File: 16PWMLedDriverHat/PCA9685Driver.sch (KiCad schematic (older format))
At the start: 17 parts, among them P1 C A0 A1 A2 A3 A4 A5 A6 A7, P2 C B0 B1 B2 B3 B4 B5 B6 B7, U1 PCA9685, U2 TBD62X83A, U3 TBD62X83A

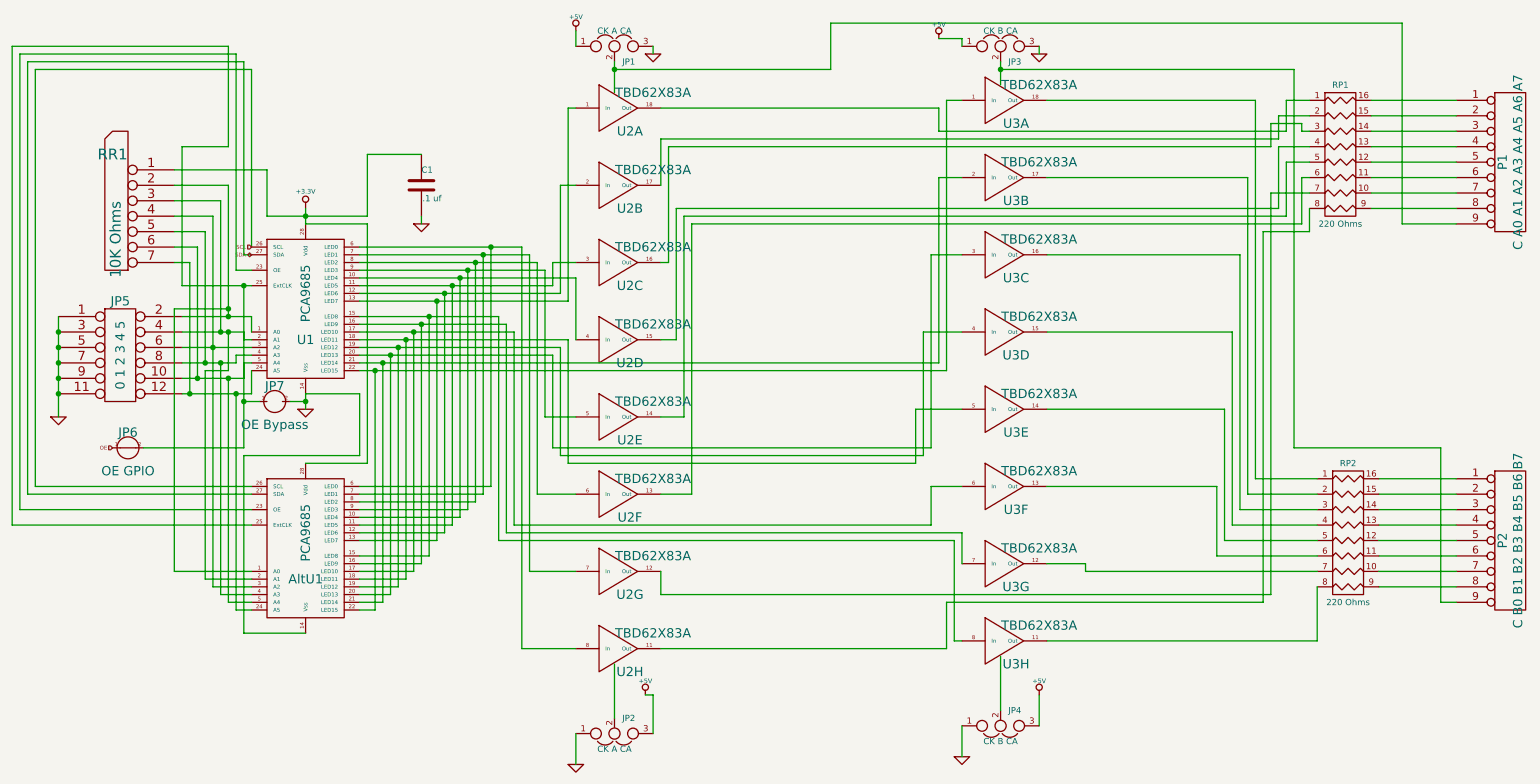
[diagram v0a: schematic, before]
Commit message: Convert the 16PWM Led Drivers to use 12V for the LEDs.
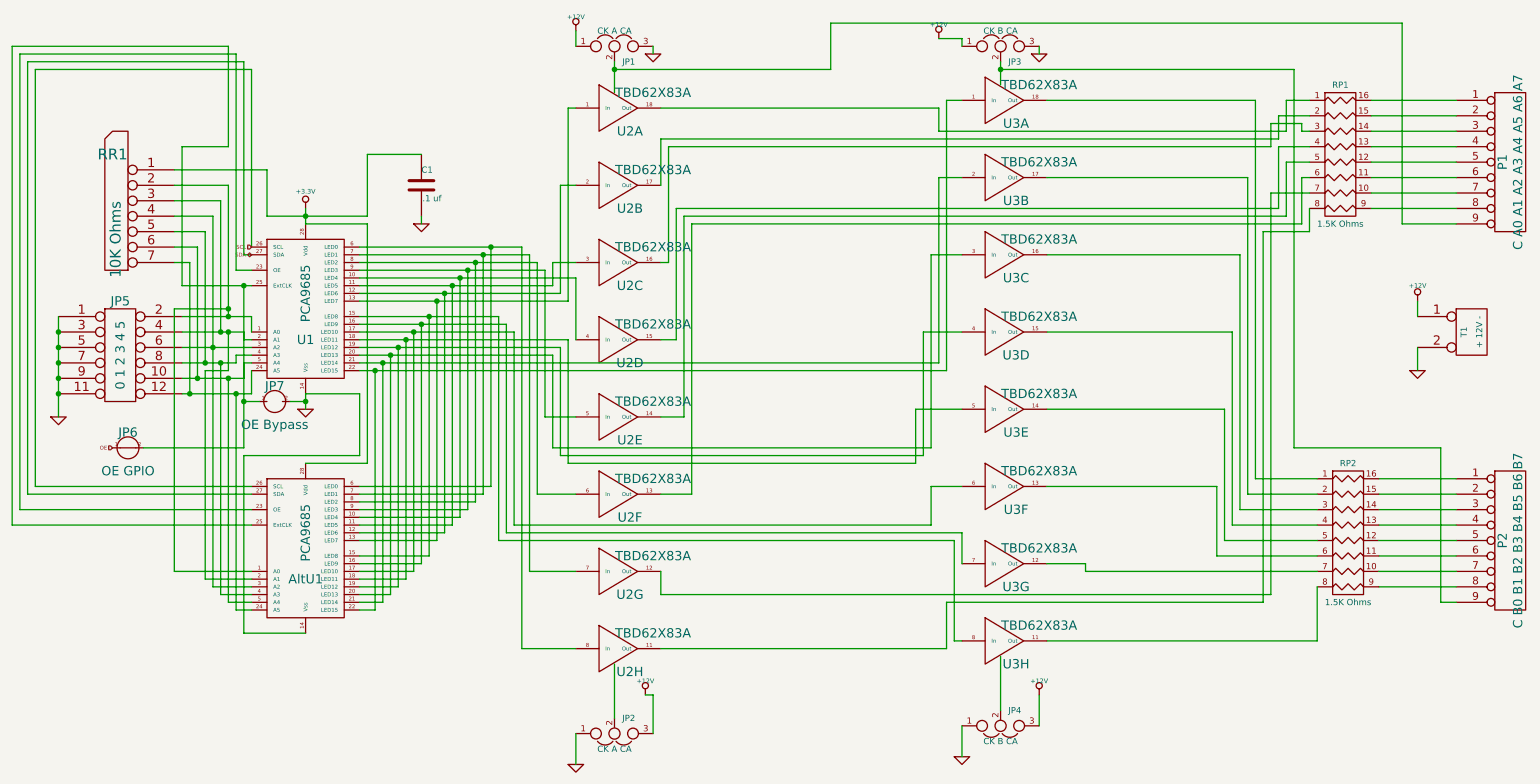
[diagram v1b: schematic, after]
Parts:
- added T1: + 12V -, symbol CONN_2
- RP1, RP2: value 220 Ohms -> 1.5K Ohms
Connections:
- net GND: now also T1.2 (PM)
- net +5V renamed +12V
- net +12V: now also T1.1 (P1)
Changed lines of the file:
@@
 Sheet 2 2
 Title ""
-Date "10 mar 2019"
+Date "28 mar 2019"
 Rev ""
 Comp ""
@@
 P 9500 1400
 F 0 "RP1" H 9500 1850 40  0000 C CNN
-F 1 "220 Ohms" H 9500 950 40  0000 C CNN
+F 1 "1.5K Ohms" H 9500 950 40  0000 C CNN
 F 2 "~" H 9500 1400 60  0000 C CNN
 F 3 "~" H 9500 1400 60  0000 C CNN
@@
 P 9550 3850
 F 0 "RP2" H 9550 4300 40  0000 C CNN
-F 1 "220 Ohms" H 9550 3400 40  0000 C CNN
+F 1 "1.5K Ohms" H 9550 3400 40  0000 C CNN
 F 2 "~" H 9550 3850 60  0000 C CNN
 F 3 "~" H 9550 3850 60  0000 C CNN
@@
 $EndComp
 $Comp
-L +5V #PWR07
+L +12V #PWR07
 U 1 1 5C84283A
 P 4550 600
 F 0 "#PWR07" H 4550 690 20  0001 C CNN
-F 1 "+5V" H 4550 690 30  0000 C CNN
+F 1 "+12V" H 4550 690 30  0000 C CNN
 F 2 "" H 4550 600 60  0000 C CNN
 F 3 "" H 4550 600 60  0000 C CNN
@@
 $EndComp
 $Comp
-L +5V #PWR08
+L +12V #PWR08
 U 1 1 5C842849
 P 6900 650
 F 0 "#PWR08" H 6900 740 20  0001 C CNN
-F 1 "+5V" H 6900 740 30  0000 C CNN
+F 1 "+12V" H 6900 740 30  0000 C CNN
 F 2 "" H 6900 650 60  0000 C CNN
 F 3 "" H 6900 650 60  0000 C CNN
@@
 $EndComp
 $Comp
-L +5V #PWR09
+L +12V #PWR09
 U 1 1 5C842858
 P 7550 4900
 F 0 "#PWR09" H 7550 4990 20  0001 C CNN
-F 1 "+5V" H 7550 4990 30  0000 C CNN
+F 1 "+12V" H 7550 4990 30  0000 C CNN
 F 2 "" H 7550 4900 60  0000 C CNN
 F 3 "" H 7550 4900 60  0000 C CNN
@@
 $EndComp
 $Comp
-L +5V #PWR010
+L +12V #PWR010
 U 1 1 5C842867
 P 5000 4900
 F 0 "#PWR010" H 5000 4990 20  0001 C CNN
-F 1 "+5V" H 5000 4990 30  0000 C CNN
+F 1 "+12V" H 5000 4990 30  0000 C CNN
 F 2 "" H 5000 4900 60  0000 C CNN
 F 3 "" H 5000 4900 60  0000 C CNN
@@
 	4550 1600 4450 1600
 Wire Wire Line
-	4450 2300 4450 1600
-Wire Wire Line
-	3150 2300 4450 2300
+	4450 1600 4450 2300
+Wire Wire Line
+	4450 2300 3150 2300
 Wire Wire Line
 	3150 2250 4400 2250
@@
 	4550 3600 4300 3600
 Wire Wire Line
-	4300 2100 4300 3600
-Wire Wire Line
-	3150 2100 4300 2100
+	4300 3600 4300 2100
+Wire Wire Line
+	4300 2100 3150 2100
 Wire Wire Line
 	4200 4600 4550 4600
@@
 	7050 1550 6900 1550
 Wire Wire Line
-	6900 2750 6900 1550
-Wire Wire Line
-	3150 2750 6900 2750
+	6900 1550 6900 2750
+Wire Wire Line
+	6900 2750 3150 2750
 Wire Wire Line
 	3150 2700 4400 2700
@@
 	6800 3350 4450 3350
 Wire Wire Line
-	4450 2650 4450 3350
-Wire Wire Line
-	3150 2650 4450 2650
+	4450 3350 4450 2650
+Wire Wire Line
+	4450 2650 3150 2650
 Wire Wire Line
 	3150 2600 4500 2600
@@
 	6850 3800 4150 3800
 Wire Wire Line
-	4150 2550 4150 3800
-Wire Wire Line
-	3150 2550 4150 2550
+	4150 3800 4150 2550
+Wire Wire Line
+	4150 2550 3150 2550
 Wire Wire Line
 	3150 2500 4100 2500
@@
 	7000 3900 4050 3900
 Wire Wire Line
-	4050 2450 4050 3900
-Wire Wire Line
-	3150 2450 4050 2450
+	4050 3900 4050 2450
+Wire Wire Line
+	4050 2450 3150 2450
 Wire Wire Line
 	4800 800  4800 1000
@@
 	2450 2600 2400 2600
 Wire Wire Line
-	2400 2550 2400 2600
-Wire Wire Line
-	2000 2550 2400 2550
+	2400 2600 2400 2550
+Wire Wire Line
+	2400 2550 2000 2550
 Wire Wire Line
 	2450 2750 2400 2750
 Wire Wire Line
-	2400 2850 2400 2750
-Wire Wire Line
-	2000 2850 2400 2850
+	2400 2750 2400 2850
+Wire Wire Line
+	2400 2850 2000 2850
 Wire Wire Line
 	2450 2700 2350 2700
 Wire Wire Line
-	2350 2750 2350 2700
-Wire Wire Line
-	2000 2750 2350 2750
+	2350 2700 2350 2750
+Wire Wire Line
+	2350 2750 2000 2750
 Wire Wire Line
 	2000 2650 2450 2650
@@
 	2500 3000 2400 3000
 Connection ~ 2400 3000
+$Comp
+L CONN_2 T1
+U 1 1 5C9CC595
+P 10350 2550
+F 0 "T1" V 10300 2550 40  0000 C CNN
+F 1 "+ 12V -" V 10400 2550 40  0000 C CNN
+F 2 "" H 10350 2550 60  0000 C CNN
+F 3 "" H 10350 2550 60  0000 C CNN
+	1    10350 2550
+	1    0    0    -1
+$EndComp
+$Comp
+L +12V #PWR016
+U 1 1 5C9CC5B0
+P 10000 2350
+F 0 "#PWR016" H 10000 2300 20  0001 C CNN
+F 1 "+12V" H 10000 2450 30  0000 C CNN
+F 2 "" H 10000 2350 60  0000 C CNN
+F 3 "" H 10000 2350 60  0000 C CNN
+	1    10000 2350
+	1    0    0    -1
+$EndComp
+$Comp
+L GND #PWR017
+U 1 1 5C9CC5BF
+P 10000 2800
+F 0 "#PWR017" H 10000 2800 30  0001 C CNN
+F 1 "GND" H 10000 2730 30  0001 C CNN
+F 2 "" H 10000 2800 60  0000 C CNN
+F 3 "" H 10000 2800 60  0000 C CNN
+	1    10000 2800
+	1    0    0    -1
+$EndComp
+Wire Wire Line
+	10000 2650 10000 2800
+Wire Wire Line
+	10000 2450 10000 2350
 $EndSCHEMATC

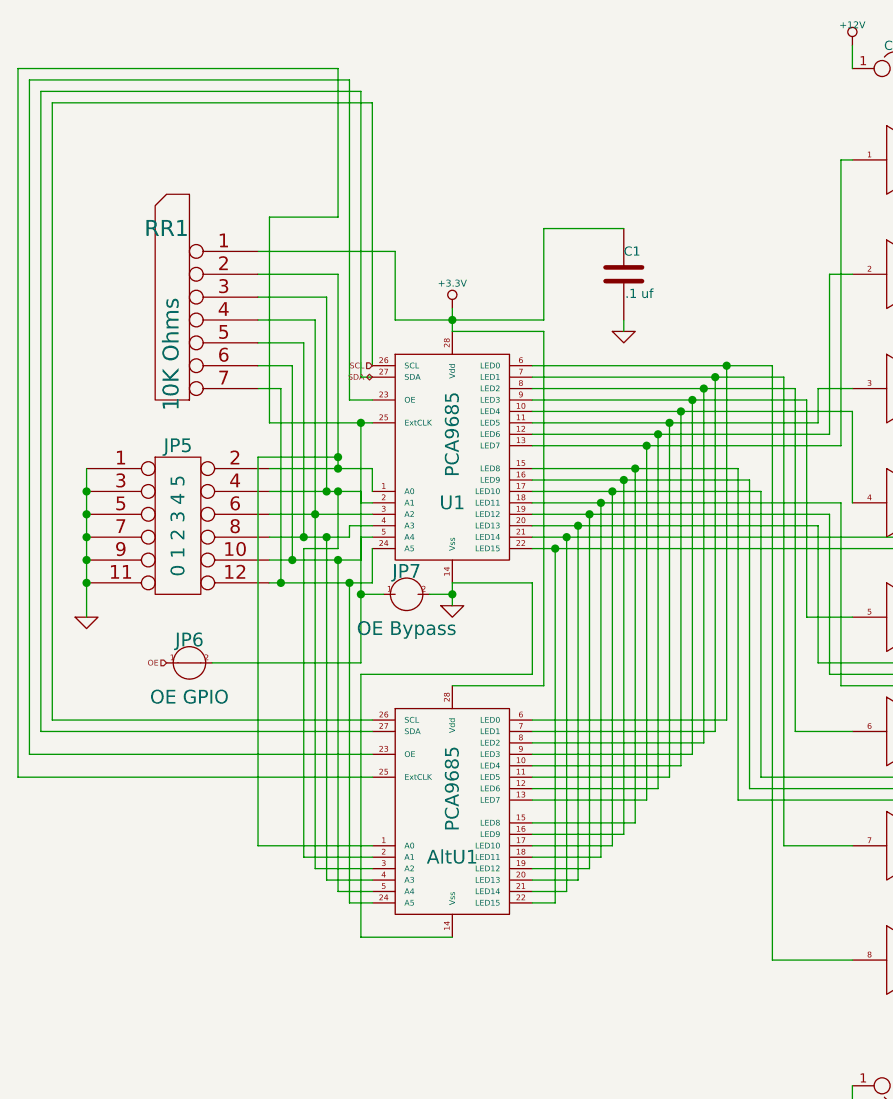
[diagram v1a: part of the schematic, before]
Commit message: Remove unnecessary DIP from 16PWMLedDriverHat.
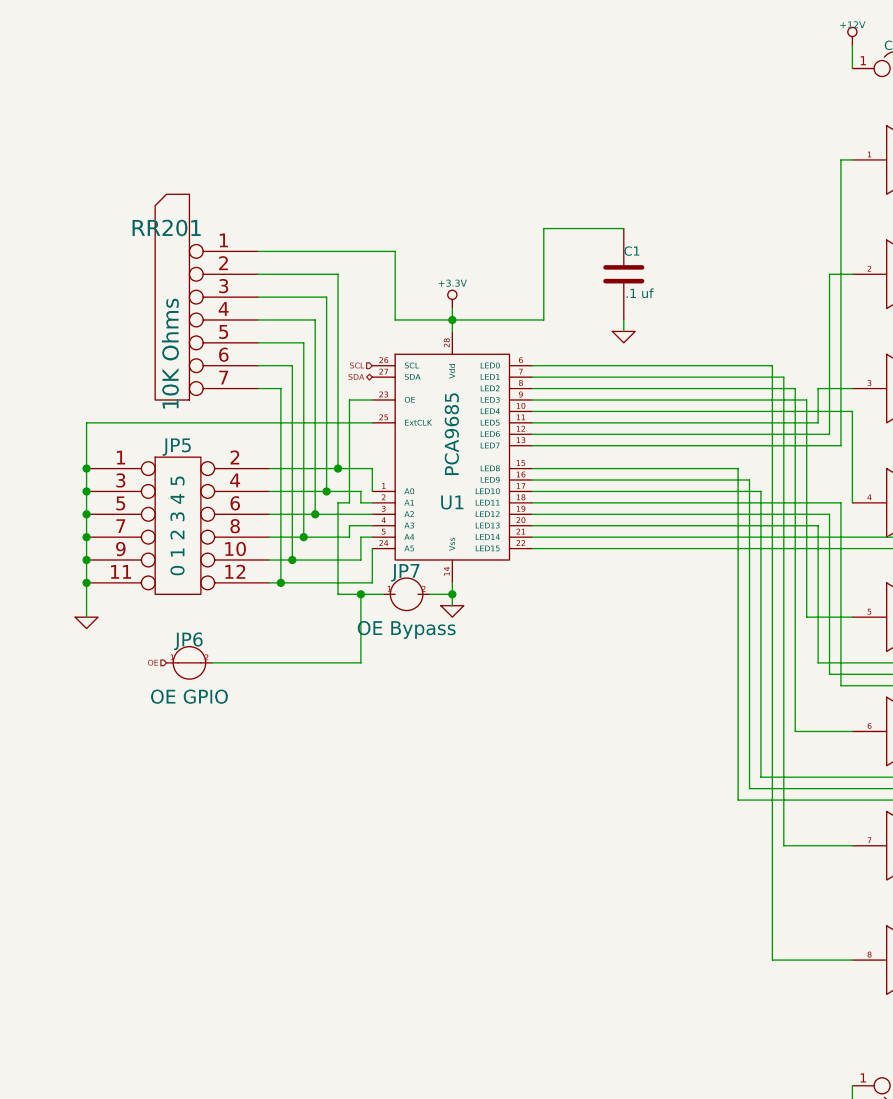
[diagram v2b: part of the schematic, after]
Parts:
- removed AltU1: PCA9685, ~, symbol PCA9685
- removed RR1: 10K Ohms, ~, symbol RR6
- added RR201: 10K Ohms, ~, symbol RR6
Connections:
- net +3.3V: now also RR201.1 (COM)
- net GND: now also U1.25 (ExtCLK)
- net at JP5.2 (P2), U1.1 (A0): now also RR201.2
- net at U1.23 (OE): now also JP6.2, JP7.1
- net at JP5.12, U1.24 (A5): now also RR201.7
- net at JP5.6 (P6), U1.3 (A2): now also RR201.4
- net at JP5.8 (P8), U1.4 (A3): now also RR201.5
- new net: JP5.4 (P4), RR201.3, U1.2 (A1)
- new net: JP5.10, RR201.6, U1.5 (A4)
